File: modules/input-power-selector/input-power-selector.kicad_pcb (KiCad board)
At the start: 2 copper layers, 27 parts, among them Q1 SI4909DY-T1-GE3, Q2 SI4909DY-T1-GE3, Q3 SI4909DY-T1-GE3, Q4 IPF067N20NM6ATMA1, Q5 BC547, U1 LTC4417IGN

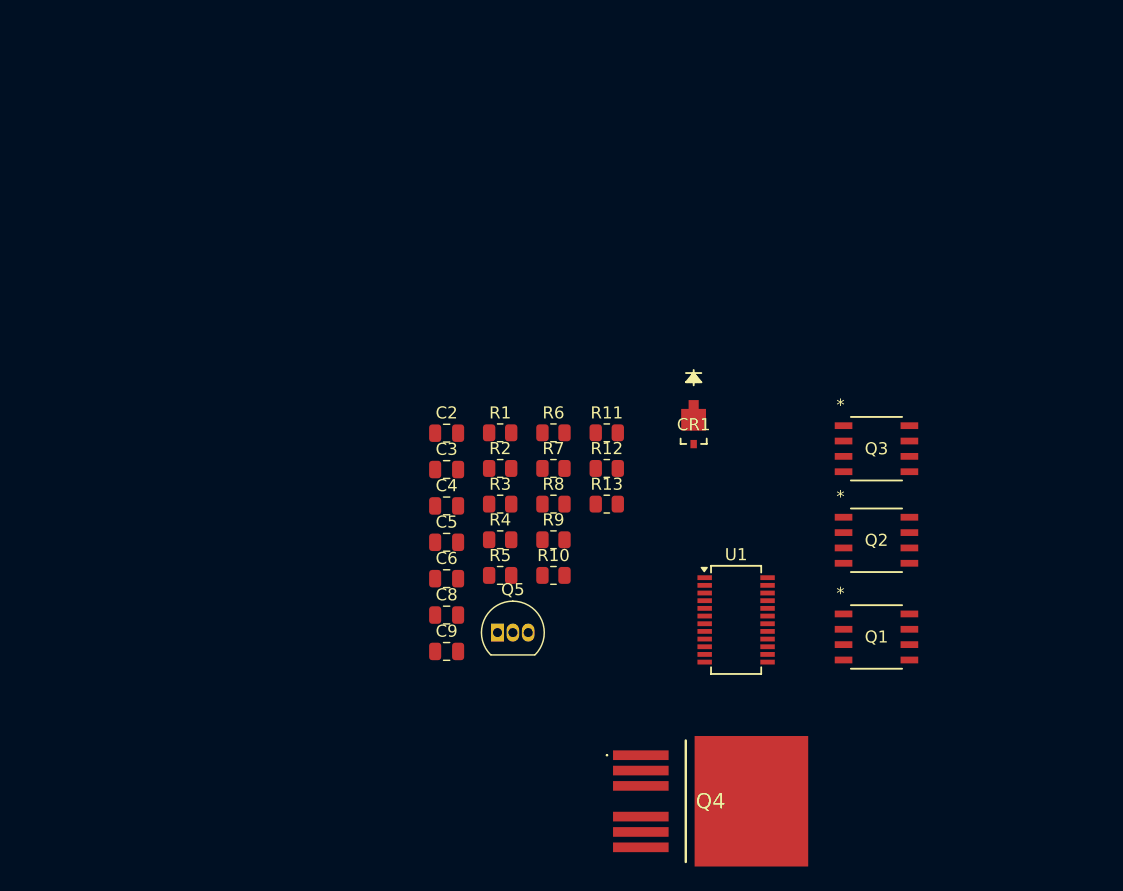
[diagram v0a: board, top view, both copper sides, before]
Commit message: work on laying out power input selector
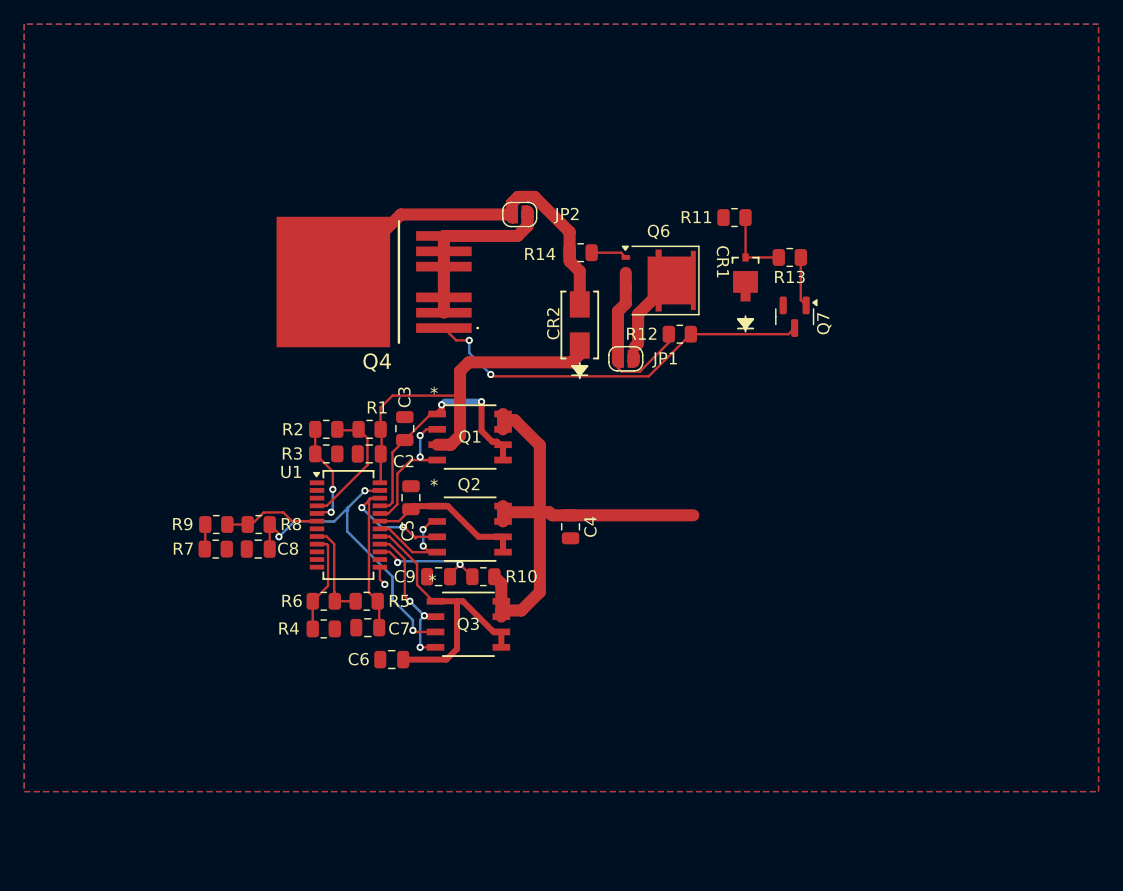
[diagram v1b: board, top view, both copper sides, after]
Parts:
- removed Q5: BC547, Package_TO_SOT_THT:TO-92_Inline
- added C7: 0.1uF, Capacitor_SMD:C_0805_2012Metric, F.Cu at (41.1, 62.6)
- added CR2: SMCJ33A, footprints:DIODE_DO-214AC, F.Cu at (58.7, 37.6)
- added JP1: Jumper_2_Open, Jumper:SolderJumper-2_P1.3mm_Open_RoundedPad1.0x1.5mm, F.Cu at (62.5, 40.4)
- added JP2: Jumper_2_Open, Jumper:SolderJumper-2_P1.3mm_Open_RoundedPad1.0x1.5mm, F.Cu at (53.7, 28.4)
- added Q6: SQJQ457EP, Package_SO:PowerPAK_SO-8L_Single, F.Cu at (65.2, 33.9)
- added Q7: BC847, Package_TO_SOT_SMD:SOT-23, F.Cu at (76.5, 36.9)
- added R14: 246K 0.25W, Resistor_SMD:R_0805_2012Metric, F.Cu at (58.7, 31.6)
- moved Q4 51.2 mm to (41.7, 34.0), turned to 0 degrees
- moved Q1 37.5 mm to (49.6, 46.9)
- moved Q3 36.8 mm to (49.5, 62.4)
- moved Q2 33.6 mm to (49.6, 54.5)
- moved U1 33.0 mm to (39.5, 54.1)
- moved R7 28.7 mm to (28.6, 56.1), turned to 180 degrees
- moved R9 27.9 mm to (28.6, 54.1), turned to 180 degrees
- moved R13 25.4 mm to (76.0, 32.0), turned to 180 degrees
- moved R8 24.4 mm to (32.1, 54.1), turned to 180 degrees
- moved R6 23.6 mm to (37.5, 60.5), turned to 180 degrees
- moved R11 20.7 mm to (71.5, 28.7), turned to 180 degrees
- moved C8 16.5 mm to (32.1, 56.1)
- moved R4 16.4 mm to (37.5, 62.7), turned to 180 degrees
- moved R3 15.0 mm to (37.7, 48.3), turned to 180 degrees
- moved R2 14.7 mm to (37.7, 46.2), turned to 180 degrees
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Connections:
- C2 pad 2: DIRTY_DC_+ -> DIRTY_DC_+_PROTECTED
- C3 pad 1: Net-(Q1-S2) -> Net-(Q1-S1)
- C5 pad 1: Net-(Q2-S2) -> Net-(Q2-S1)
- C6 pad 1: Net-(Q3-S2) -> Net-(Q3-S1)
- CR1 pad 1: DIRTY_DC_+ -> DIRTY_DC_+_PROTECTED
- Q1 pad 1: DIRTY_DC_+ -> Net-(Q1-S1)
- Q1 pad 3: Net-(Q1-S2) -> DIRTY_DC_+_PROTECTED
- Q1 pad 5: Net-(Q1-S2) -> Net-(Q1-S1)
- Q1 pad 6: Net-(Q1-S2) -> Net-(Q1-S1)
- Q2 pad 1: USB-C_POWER_IN -> Net-(Q2-S1)
- Q2 pad 3: Net-(Q2-S2) -> USB-C_POWER_IN
- Q2 pad 5: Net-(Q2-S2) -> Net-(Q2-S1)
- Q2 pad 6: Net-(Q2-S2) -> Net-(Q2-S1)
- Q3 pad 1: INTERNAL_SOLAR_IN -> Net-(Q3-S1)
- Q3 pad 3: Net-(Q3-S2) -> INTERNAL_SOLAR_IN
- Q3 pad 5: Net-(Q3-S2) -> Net-(Q3-S1)
- Q3 pad 6: Net-(Q3-S2) -> Net-(Q3-S1)
- R1 pad 1: DIRTY_DC_+ -> DIRTY_DC_+_PROTECTED
- R11 pad 2: unconnected-(R11-Pad2) -> GND
- U1 pad 17: Net-(Q3-S2) -> Net-(Q3-S1)
- U1 pad 19: Net-(Q2-S2) -> Net-(Q2-S1)
- U1 pad 21: Net-(Q1-S2) -> Net-(Q1-S1)
- U1 pad 24: DIRTY_DC_+ -> DIRTY_DC_+_PROTECTED
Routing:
- net VOUT: track 0.00 -> 41.8 mm
- net DIRTY_DC_+_PROTECTED: track 0.00 -> 40.1 mm
- net Net-(Q4-G): track 0.00 -> 33.0 mm, vias 0 -> 2
- net DIRTY_DC_-: track 0.00 -> 30.6 mm
- net INTERNAL_SOLAR_IN: track 0.00 -> 28.2 mm, vias 0 -> 3
- net Net-(Q3-S1): track 0.00 -> 24.4 mm
- net Net-(Q1-S1): track 0.00 -> 21.8 mm, vias 0 -> 2
- net USB-C_POWER_IN: track 0.00 -> 21.3 mm, vias 0 -> 2
- net GND: track 0.00 -> 16.2 mm, vias 0 -> 1
- net DIRTY_DC_+: track 0.00 -> 14.2 mm
- net Net-(Q2-S1): track 0.00 -> 13.0 mm
- net Net-(Q1-G1): track 0.00 -> 13.0 mm, vias 0 -> 2
- net Net-(Q3-G1): track 0.00 -> 12.9 mm, vias 0 -> 3
- net Net-(U1-UV1): track 0.00 -> 10.6 mm
- net VOUT_PIN: track 0.00 -> 10.1 mm, vias 0 -> 2
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- added copper zone on B.Cu, net GND
- added copper zone on F.Cu, net GND
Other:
- board text added: "IPF067N20NM6ATMA1"

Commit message: more layout fixing on power selector
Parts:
- added D1: BZX384-C30_115, footprints:DIO_BZX384-C30_115, F.Cu at (76.7, 40.6)
- added D2: BZX384-C30_115, footprints:DIO_BZX384-C30_115, F.Cu at (71.0, 40.6)
- added D3: BZX384-C12_115, footprints:DIO_BZX384-C30_115, F.Cu at (61.6, 27.9)
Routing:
- net DIRTY_DC_+_PROTECTED: track 40.1 -> 57.6 mm
- net /OVERVOLTAGE_SENSE_CLAMPED: track 6.05 -> 20.2 mm
- net GND: track 16.2 -> 29.8 mm, vias 1 -> 6
- net Net-(U1-OV2): track 2.05 -> 14.4 mm
- net Net-(Q4-G): track 33.0 -> 44.0 mm
- net DIRTY_DC_+: track 14.2 -> 21.4 mm, vias 0 -> 2
- net Net-(Q6-G): track 2.99 -> 7.01 mm
- net Net-(Q1-S1): track 21.8 -> 23.9 mm

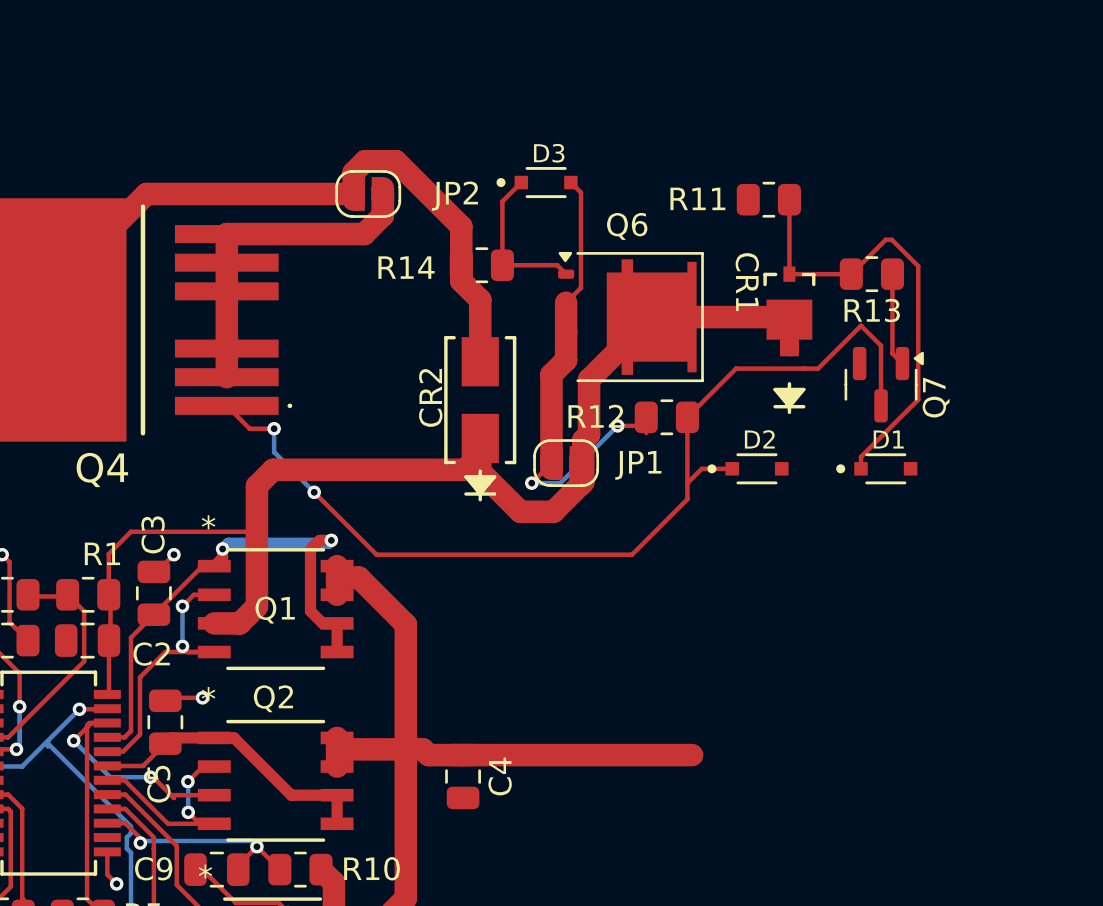
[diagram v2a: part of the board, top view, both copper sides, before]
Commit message: update input source selecter PCB layout
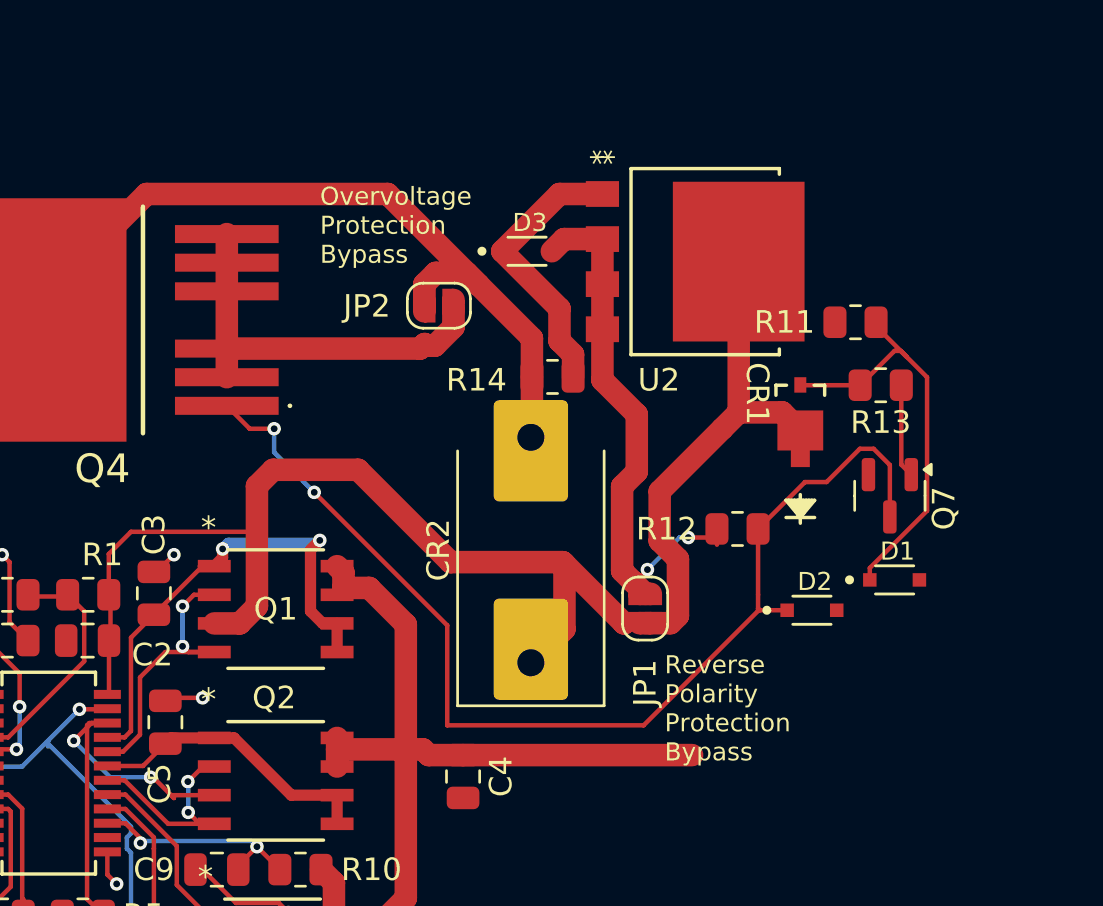
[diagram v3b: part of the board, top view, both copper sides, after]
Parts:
- removed Q6: SQJQ457EP, Package_SO:PowerPAK_SO-8L_Single
- added U2: SQJQ141EL-T1_GE3, footprints:PowerPAK_8x8L_BWL-2_VIS, F.Cu at (68.7, 31.4)
- CR2: footprint footprints:DIODE_DO-214AC -> Diode_SMD:D_SMC-RM10_Universal_Handsoldering
- moved JP1 7.34 mm to (66.0, 46.8), turned to 90 degrees
- moved CR2 7.02 mm to (60.9, 44.2)
- moved D2 6.73 mm to (73.4, 46.9)
- moved R11 6.66 mm to (75.3, 34.1)
- moved JP2 5.86 mm to (56.8, 33.4)
- moved R12 5.86 mm to (70.1, 43.3)
- moved R14 5.86 mm to (61.9, 36.6)
- moved Q7 4.94 mm to (76.8, 41.8)
- moved R13 4.94 mm to (76.4, 36.9)
- moved D1 4.94 mm to (77.1, 45.6)
- moved CR1 4.94 mm to (72.9, 38.5)
- moved D3 3.16 mm to (60.7, 31.0)
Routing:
- net DIRTY_DC_+_PROTECTED: track 57.6 -> 67.7 mm
- net Net-(Q4-G): track 44.0 -> 49.6 mm
- net Net-(U2-G): track 7.01 -> 12.4 mm
- net DIRTY_DC_-: track 30.6 -> 35.9 mm
- net DIRTY_DC_+: track 21.4 -> 24.9 mm
- net GND: track 29.8 -> 33.1 mm
- net /OVERVOLTAGE_SENSE_CLAMPED: track 20.2 -> 19.0 mm
- net Net-(Q1-S1): track 23.9 -> 22.9 mm
- net VOUT: track 41.8 -> 41.1 mm
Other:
- board text added: "Overvoltage Protection Bypass"
- board text added: "Reverse Polarity Protection Bypass"

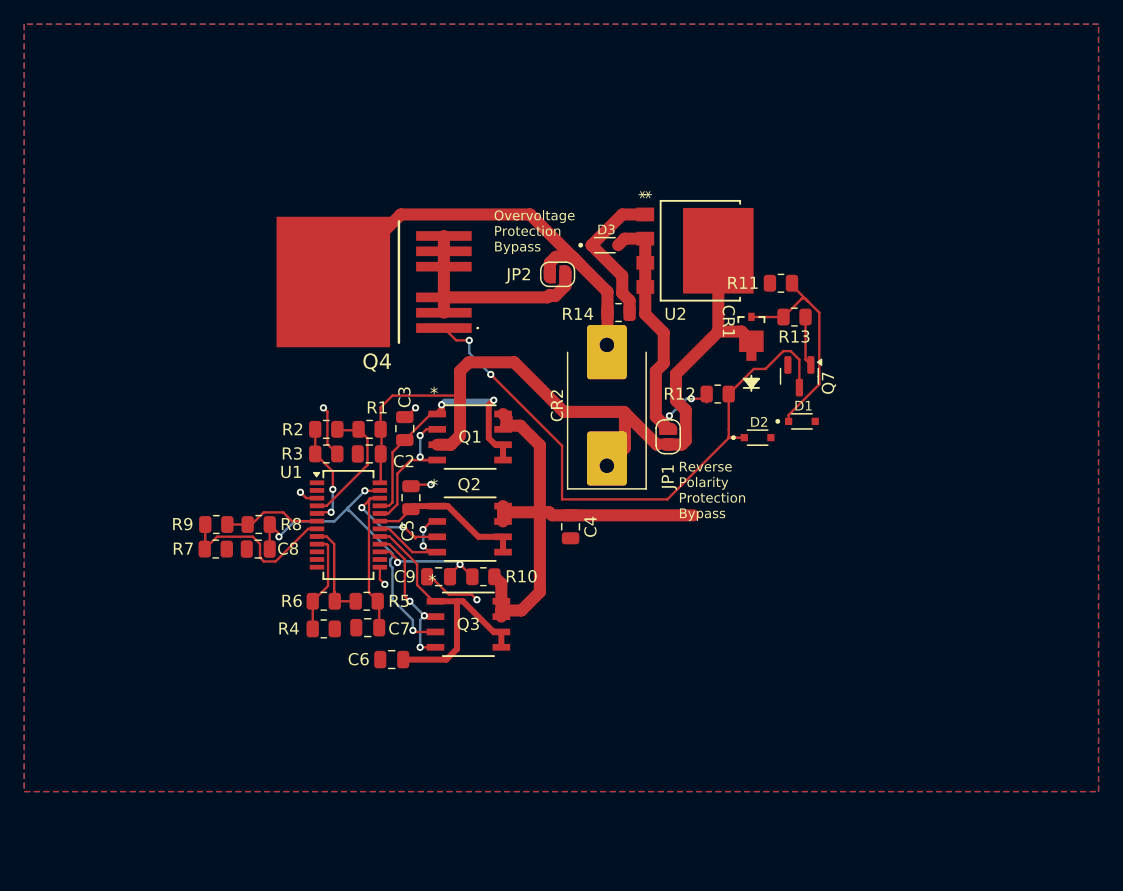
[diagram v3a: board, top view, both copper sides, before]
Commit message: add module outline for input source selecter
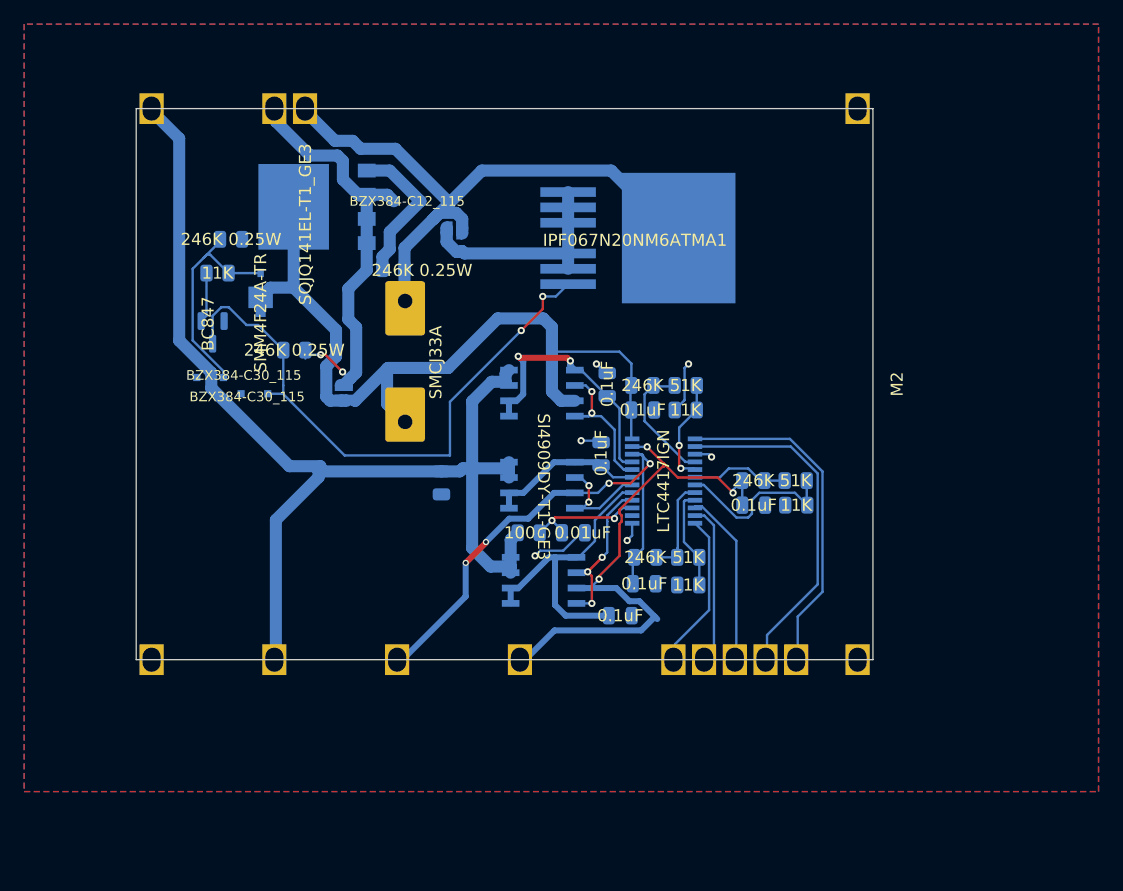
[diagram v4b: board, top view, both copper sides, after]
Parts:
- added M2: ~, MegaCastle:MegaCastle2x24-Module-I42.0x56.2-M88887D8C0001, F.Cu at (52.5, 42.5)
- C2, C3, C4, C5, C6, C7, C8, C9, CR1, CR2, D1, D2, D3, JP1, JP2, Q1, Q2, Q3, Q4, Q7, R1, R10, R11, R12, R13, R14, R2, R3, R4, R5, R6, R7, R8, R9, U1, U2: moved to B.Cu
- moved D1 49.1 mm to (28.1, 41.9), turned to 180 degrees
- moved Q7 48.7 mm to (28.3, 38.2)
- moved R7 48.2 mm to (76.6, 52.5), turned to 0 degrees
- moved R9 48.1 mm to (76.5, 50.5), turned to 0 degrees
- moved R13 47.9 mm to (28.7, 33.3), turned to 0 degrees
- moved R11 45.6 mm to (29.8, 30.5), turned to 0 degrees
- moved D2 41.8 mm to (31.8, 43.3), turned to 180 degrees
- moved C8 41.2 mm to (73.1, 52.5), turned to 180 degrees
- moved R8 41.1 mm to (73.0, 50.5), turned to 0 degrees
- moved CR1 40.8 mm to (32.3, 34.9), turned to 0 degrees
- moved R12 35.2 mm to (35.1, 39.7), turned to 180 degrees
- moved U2 32.4 mm to (36.5, 27.8)
- moved R4 30.4 mm to (67.7, 59.1), turned to 0 degrees
- moved R6 30.4 mm to (67.7, 56.8), turned to 0 degrees
- moved R2 30.0 mm to (67.4, 42.6), turned to 0 degrees
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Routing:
- net VOUT: track 41.1 -> 95.5 mm
- net /SHUTDOWN: track 0.00 -> 28.5 mm
- net ENABLE: track 0.00 -> 28.4 mm
- net USB-C_POWER_IN: track 21.3 -> 43.0 mm, vias 2 -> 4
- net INTERNAL_SOLAR_IN: track 28.4 -> 47.3 mm
- net DIRTY_DC_-: track 35.9 -> 50.8 mm
- net /VALID1: track 0.00 -> 14.9 mm
- net /VALID2: track 0.00 -> 13.6 mm
- net /VALID3: track 0.00 -> 13.3 mm
- net DIRTY_DC_+: track 24.9 -> 36.6 mm
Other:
- board outline added: 61 x 45.6 mm

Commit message: fix remaining important DRC violations
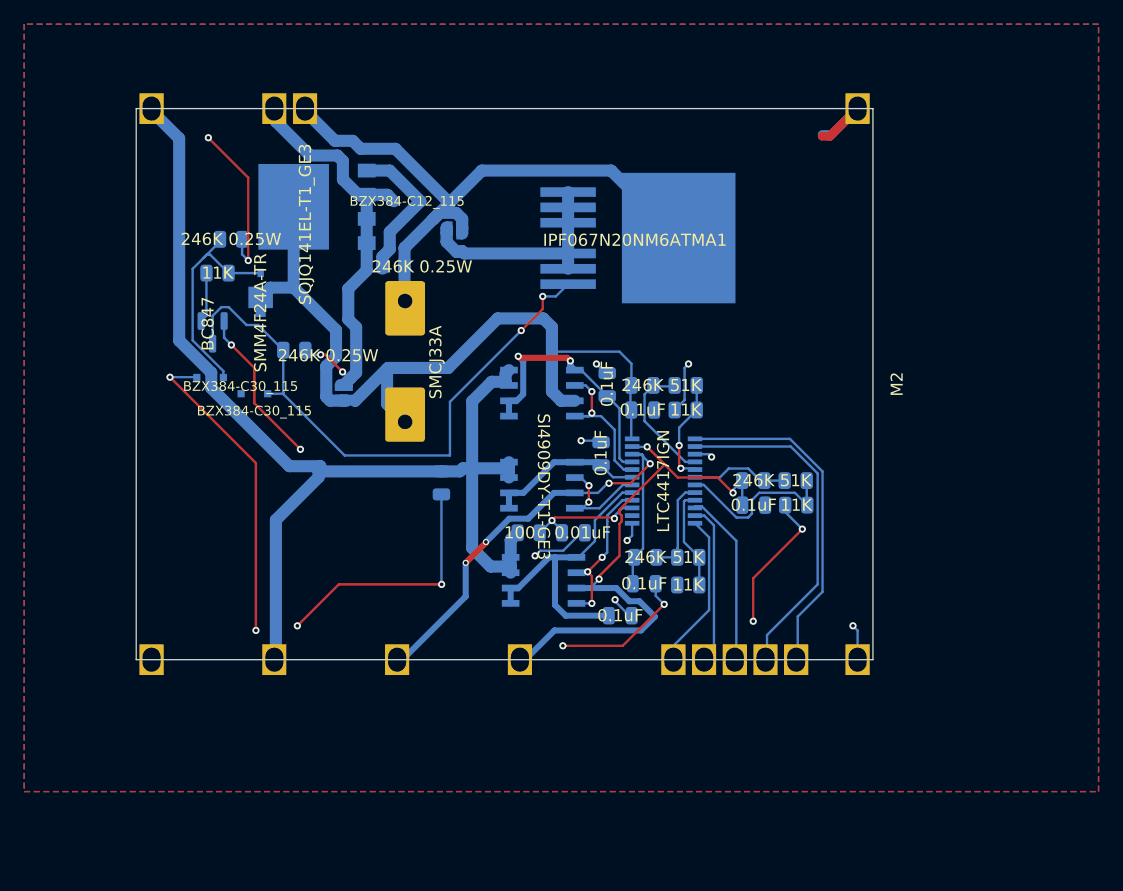
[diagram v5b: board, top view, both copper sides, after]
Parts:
- moved R14 0.29 mm to (43.3, 32.6)
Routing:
- net GND: track 33.0 -> 143.3 mm, vias 6 -> 20
- net INTERNAL_SOLAR_IN: track 47.3 -> 46.7 mm
